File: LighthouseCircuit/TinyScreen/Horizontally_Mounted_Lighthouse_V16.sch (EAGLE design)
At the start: 23 parts

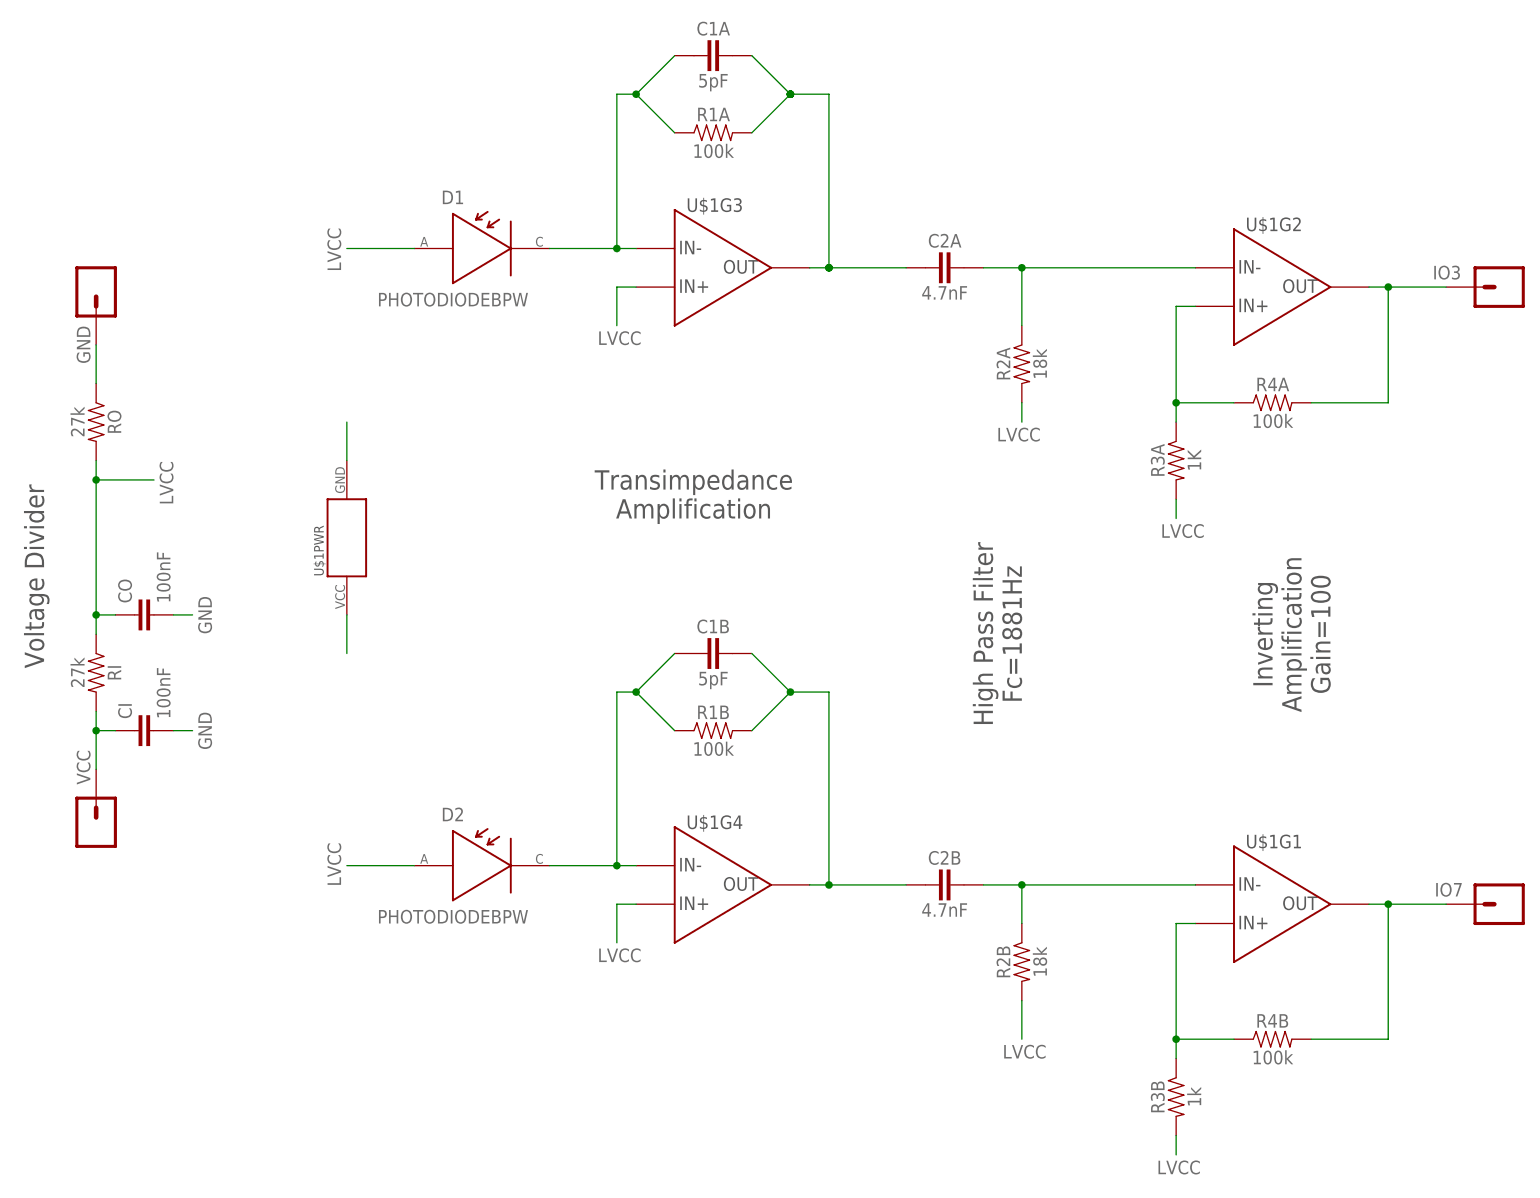
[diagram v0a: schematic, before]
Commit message: Working on initial demo of multiple Zippies in coordination.
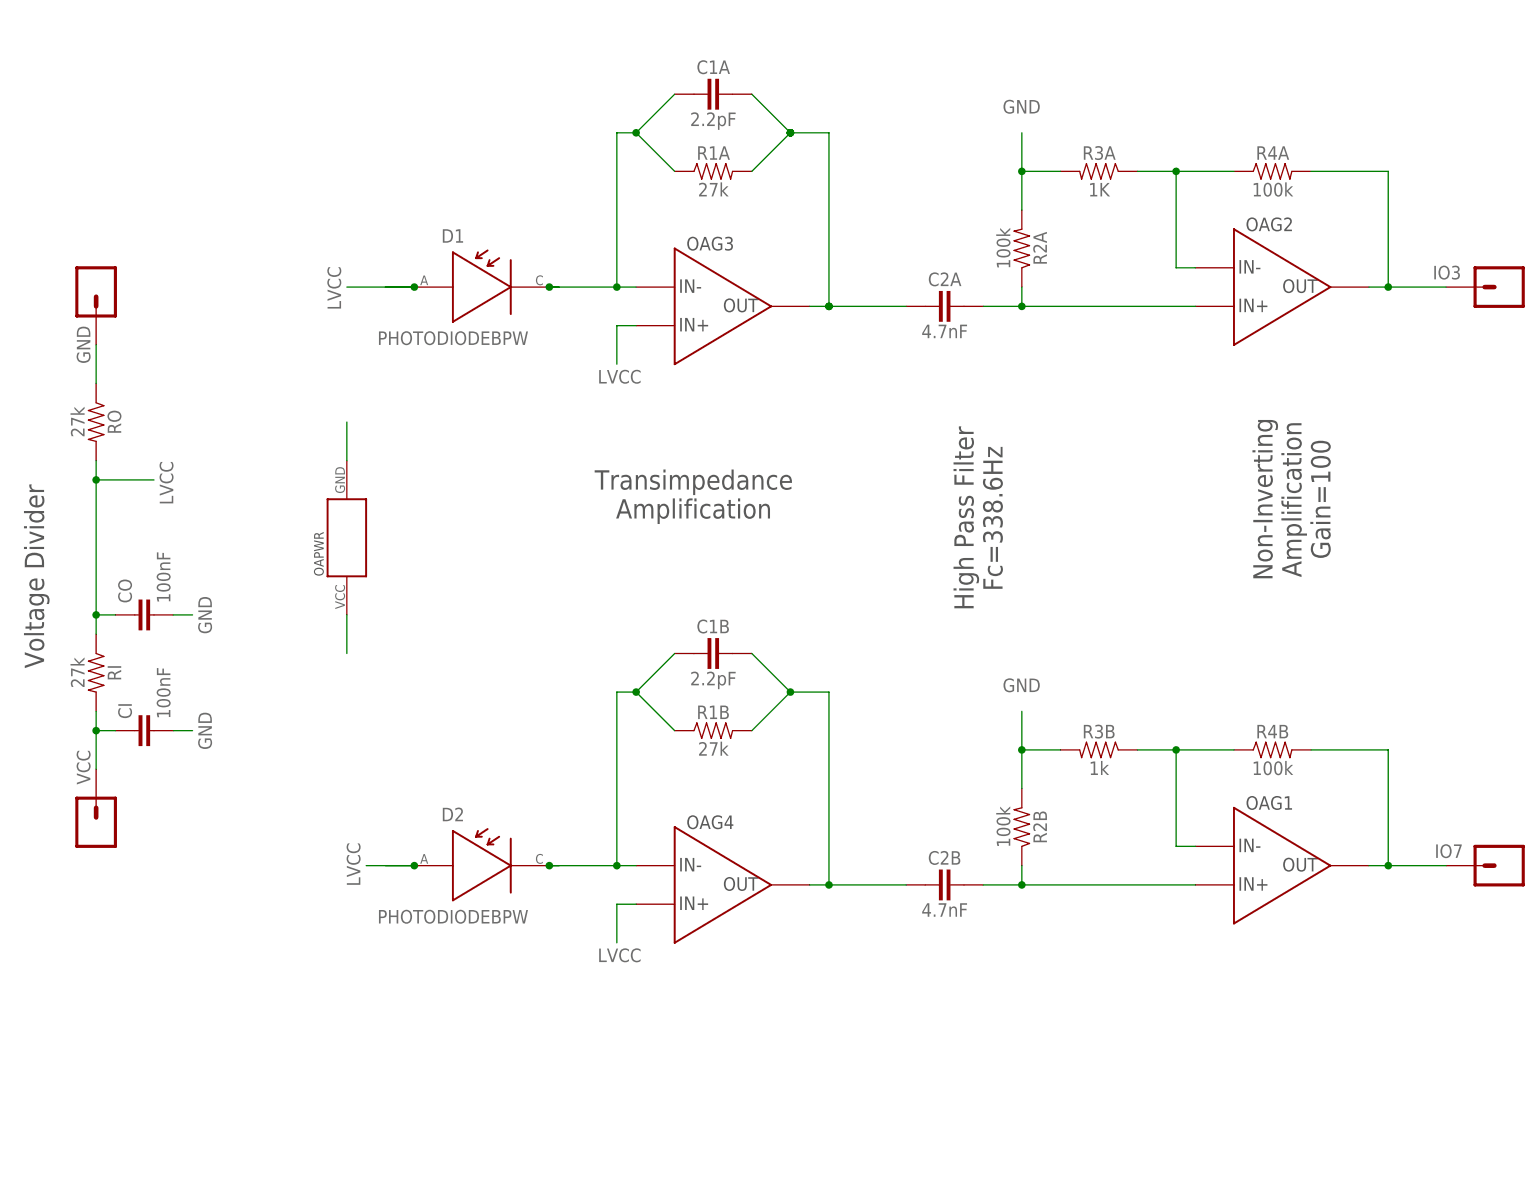
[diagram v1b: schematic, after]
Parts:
- removed U$1: TLV2464IPW, ZippyComponentLibrary:TLV2464IPW
- added OA: TLV2464IDM, ZippyComponentLibrary:TLV2464IDM
- C1A, C1B: value 5pF -> 2.2pF
- R1A, R1B: value 100k -> 27k
- R2A, R2B: value 18k -> 100k
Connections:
- removed net D2OA2N: R3A.1, R4A.1, U$1G2.IN+
- new net N$1: OAG2.IN-, R3A.1, R4A.1
- net D1IN: now also OAG4.IN-; no longer U$1G4.IN-
- net D1OA2P: now also OAG1.IN+; no longer U$1G1.IN-
- net D1OAOUT1: now also OAG4.OUT; no longer U$1G4.OUT
- net D2IN: now also OAG3.IN-; no longer U$1G3.IN-
- net D2OA1OUT: now also OAG3.OUT; no longer U$1G3.OUT
- net D2OA2P: now also OAG2.IN+; no longer U$1G2.IN-
- net GND: now also OAPWR.GND, R2A.2, R2B.2, R3A.2, R3B.2; no longer U$1PWR.GND
- net IO3: now also OAG2.OUT; no longer U$1G2.OUT
- net IO7: now also OAG1.OUT; no longer U$1G1.OUT
- net LVCC: now also OAG3.IN+, OAG4.IN+; no longer R2A.2, R2B.2, R3A.2, R3B.2, U$1G3.IN+, U$1G4.IN+
- net N$11: now also OAG1.IN-; no longer U$1G1.IN+
- net VCC: now also OAPWR.VCC; no longer U$1PWR.VCC
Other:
- note added: "High Pass Filter Fc=338.6Hz"
- note added: "Non-Inverting Amplification Gain=100"
- note removed: "High Pass Filter Fc=1881Hz"
- note removed: "Inverting Amplification Gain=100"
- moved on the sheet: C1A, C2A, D1, R1A, R2A, R2B, R3A, R3B, R4A, R4B
